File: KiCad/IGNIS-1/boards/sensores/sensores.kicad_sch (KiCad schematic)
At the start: 12 parts, among them J1 J_PWR_2x4, J41 J_DAT, U20 BME280, U21 MPU6050, U22 MQ-135, U24 GPS NEO-6M

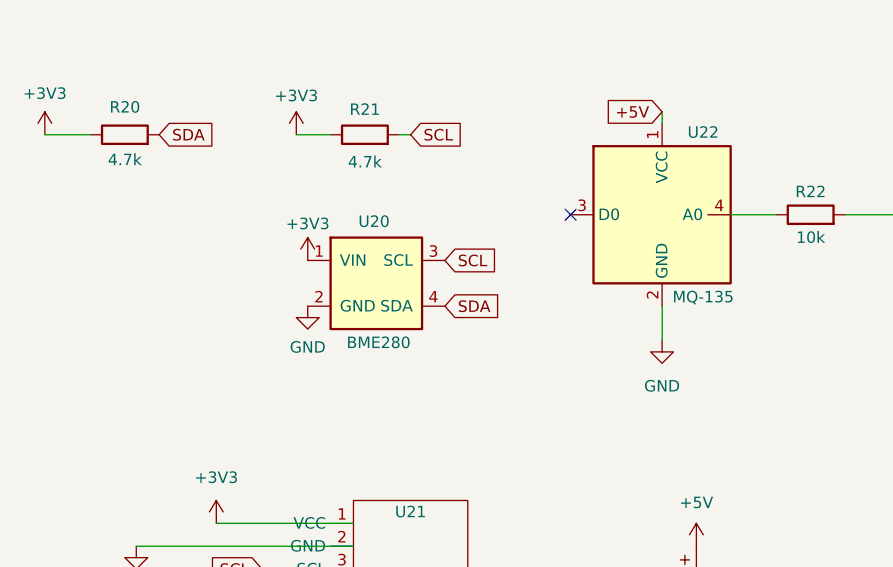
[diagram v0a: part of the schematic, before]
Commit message: Footprint BME280 propio + asignado (board sensores)
- Nuevo footprint IGNIS1:BME280_module (13.6x10.4mm, 4 THT P2.54
  VCC/GND/SCL/SDA, agujero montaje 3mm arriba-derecha).
- Asignado en simbolo maestro (default) y en instancia U20 del esquematico.
- PCB sensores: U20 cambia de PinHeader_1x04 generico a BME280_module;
  tracks viejos de U20 removidos (pads reubicados, falta rerutear).

Co-Authored-By: Claude Opus 4.8 <noreply@anthropic.com>
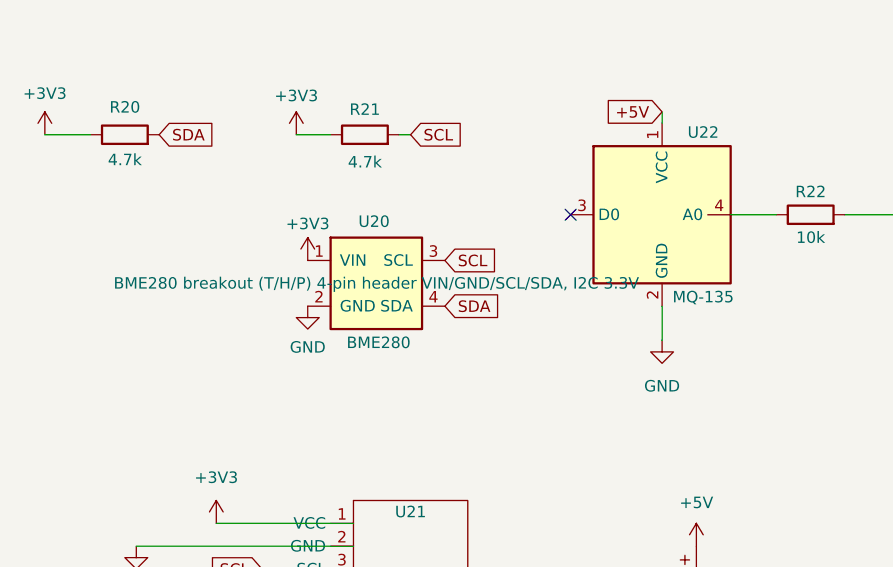
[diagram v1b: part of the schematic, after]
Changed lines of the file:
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@@
 			)
 		)
-		(property "Description" ""
+		(property "Description" "BME280 breakout (T/H/P) 4-pin header VIN/GND/SCL/SDA, I2C 3.3V"
 			(at 64.77 76.2 0)
 			(show_name no)
